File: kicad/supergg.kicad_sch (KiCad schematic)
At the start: 0 parts

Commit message: add pin connector holes
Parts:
- added U1: Cart_Connector, supergg:Cart_Connector, symbol supergg:Cart_Connector
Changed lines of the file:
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@@
 	(generator_version "9.0")
 	(paper "A4")
+	(symbol
+		(lib_id "supergg:Cart_Connector")
+		(at 72.39 88.9 0)
+		(unit 1)
+		(exclude_from_sim no)
+		(in_bom yes)
+		(on_board yes)
+		(dnp no)
+		(fields_autoplaced yes)
+		(property "Reference" "U1"
+			(at 72.39 35.56 0)
+			(effects
+				(font
+					(size 1.27 1.27)
+				)
+			)
+		)
+		(property "Value" "Cart_Connector"
+			(at 72.39 38.1 0)
+			(effects
+				(font
+					(size 1.27 1.27)
+				)
+			)
+		)
+		(property "Footprint" "supergg:Cart_Connector"
+			(at 72.39 88.9 0)
+			(effects
+				(font
+					(size 1.27 1.27)
+				)
+				(hide yes)
+			)
+		)
+		(property "Datasheet" ""
+			(at 72.39 88.9 0)
+			(effects
+				(font
+					(size 1.27 1.27)
+				)
+				(hide yes)
+			)
+		)
+		(property "Description" ""
+			(at 72.39 88.9 0)
+			(effects
+				(font
+					(size 1.27 1.27)
+				)
+				(hide yes)
+			)
+		)
+		(pin "46"
+		)
+		(pin "52"
+		)
+		(pin "8"
+		)
+		(pin "61"
+		)
+		(pin "69"
+		)
+		(pin "28"
+		)
+		(pin "24"
+		)
+		(pin "2"
+		)
+		(pin "3"
+		)
+		(pin "72"
+		)
+		(pin "33"
+		)
+		(pin "30"
+		)
+		(pin "22"
+		)
+		(pin "31"
+		)
+		(pin "34"
+		)
+		(pin "32"
+		)
+		(pin "35"
+		)
+		(pin "36"
+		)
+		(pin "59"
+		)
+		(pin "13"
+		)
+		(pin "1"
+		)
+		(pin "45"
+		)
+		(pin "70"
+		)
+		(pin "67"
+		)
+		(pin "44"
+		)
+		(pin "62"
+		)
+		(pin "20"
+		)
+		(pin "4"
+		)
+		(pin "63"
+		)
+		(pin "42"
+		)
+		(pin "7"
+		)
+		(pin "43"
+		)
+		(pin "53"
+		)
+		(pin "55"
+		)
+		(pin "18"
+		)
+		(pin "49"
+		)
+		(pin "48"
+		)
+		(pin "25"
+		)
+		(pin "12"
+		)
+		(pin "41"
+		)
+		(pin "14"
+		)
+		(pin "50"
+		)
+		(pin "16"
+		)
+		(pin "51"
+		)
+		(pin "47"
+		)
+		(pin "26"
+		)
+		(pin "15"
+		)
+		(pin "60"
+		)
+		(pin "23"
+		)
+		(pin "38"
+		)
+		(pin "54"
+		)
+		(pin "39"
+		)
+		(pin "65"
+		)
+		(pin "40"
+		)
+		(pin "68"
+		)
+		(pin "57"
+		)
+		(pin "58"
+		)
+		(pin "66"
+		)
+		(pin "19"
+		)
+		(pin "9"
+		)
+		(pin "11"
+		)
+		(pin "71"
+		)
+		(pin "10"
+		)
+		(pin "5"
+		)
+		(pin "17"
+		)
+		(pin "21"
+		)
+		(pin "29"
+		)
+		(pin "6"
+		)
+		(pin "27"
+		)
+		(pin "37"
+		)
+		(pin "64"
+		)
+		(pin "56"
+		)
+		(instances
+			(project ""
+				(path "/b7e908d3-ce0c-4aa7-87ef-800cbc8c6f17"
+					(reference "U1")
+					(unit 1)
+				)
+			)
+		)
+	)
 	(sheet_instances
 		(path "/"

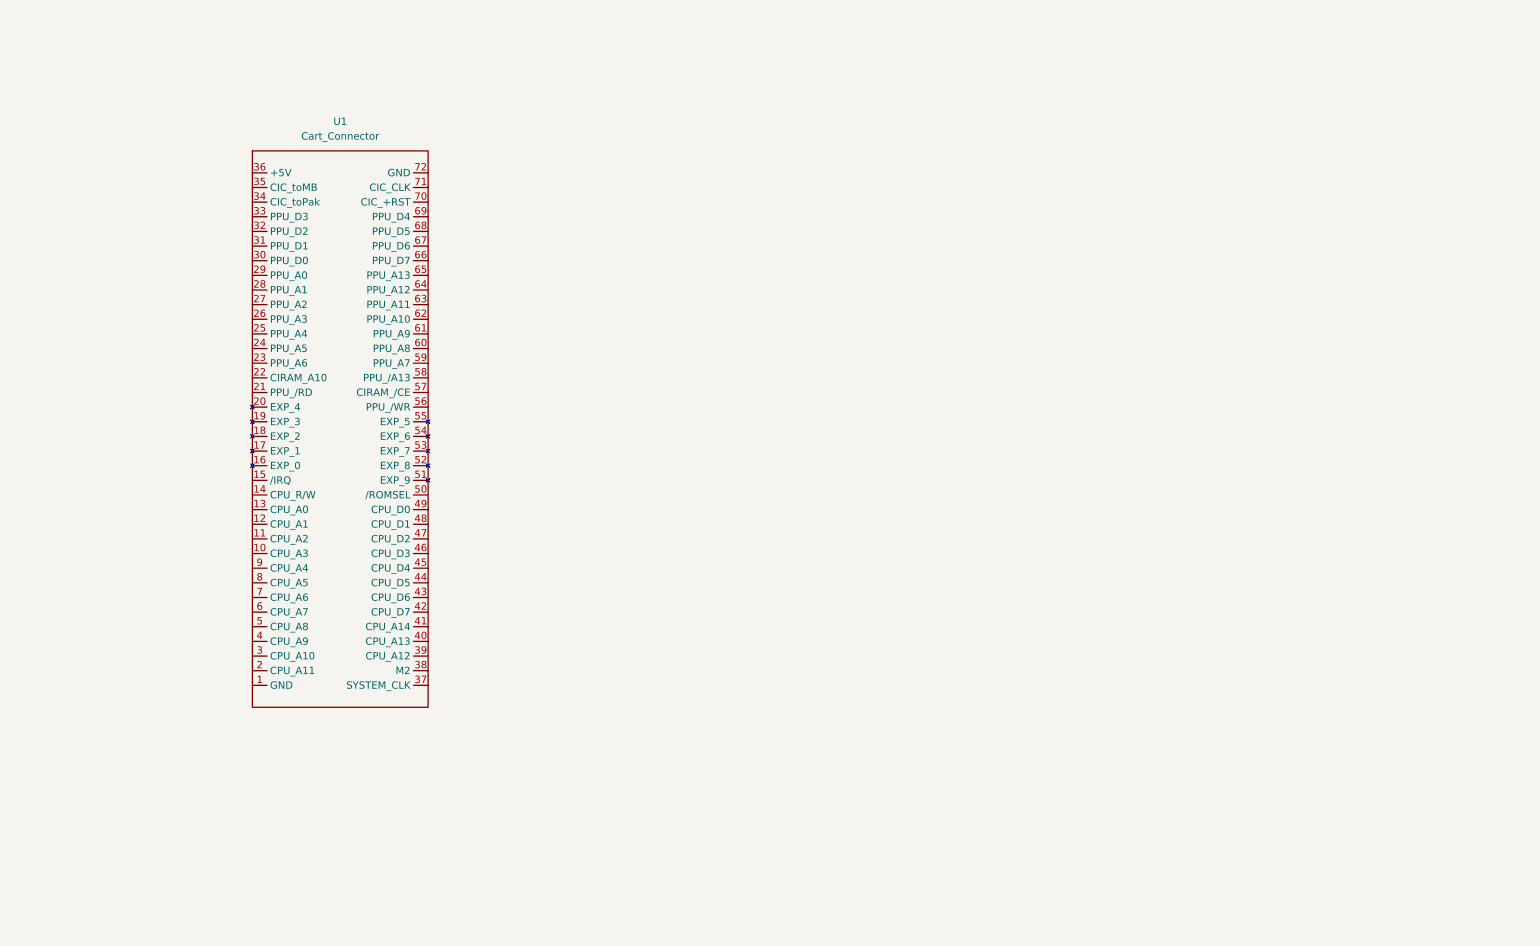
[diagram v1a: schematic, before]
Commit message: add edge connector symbol
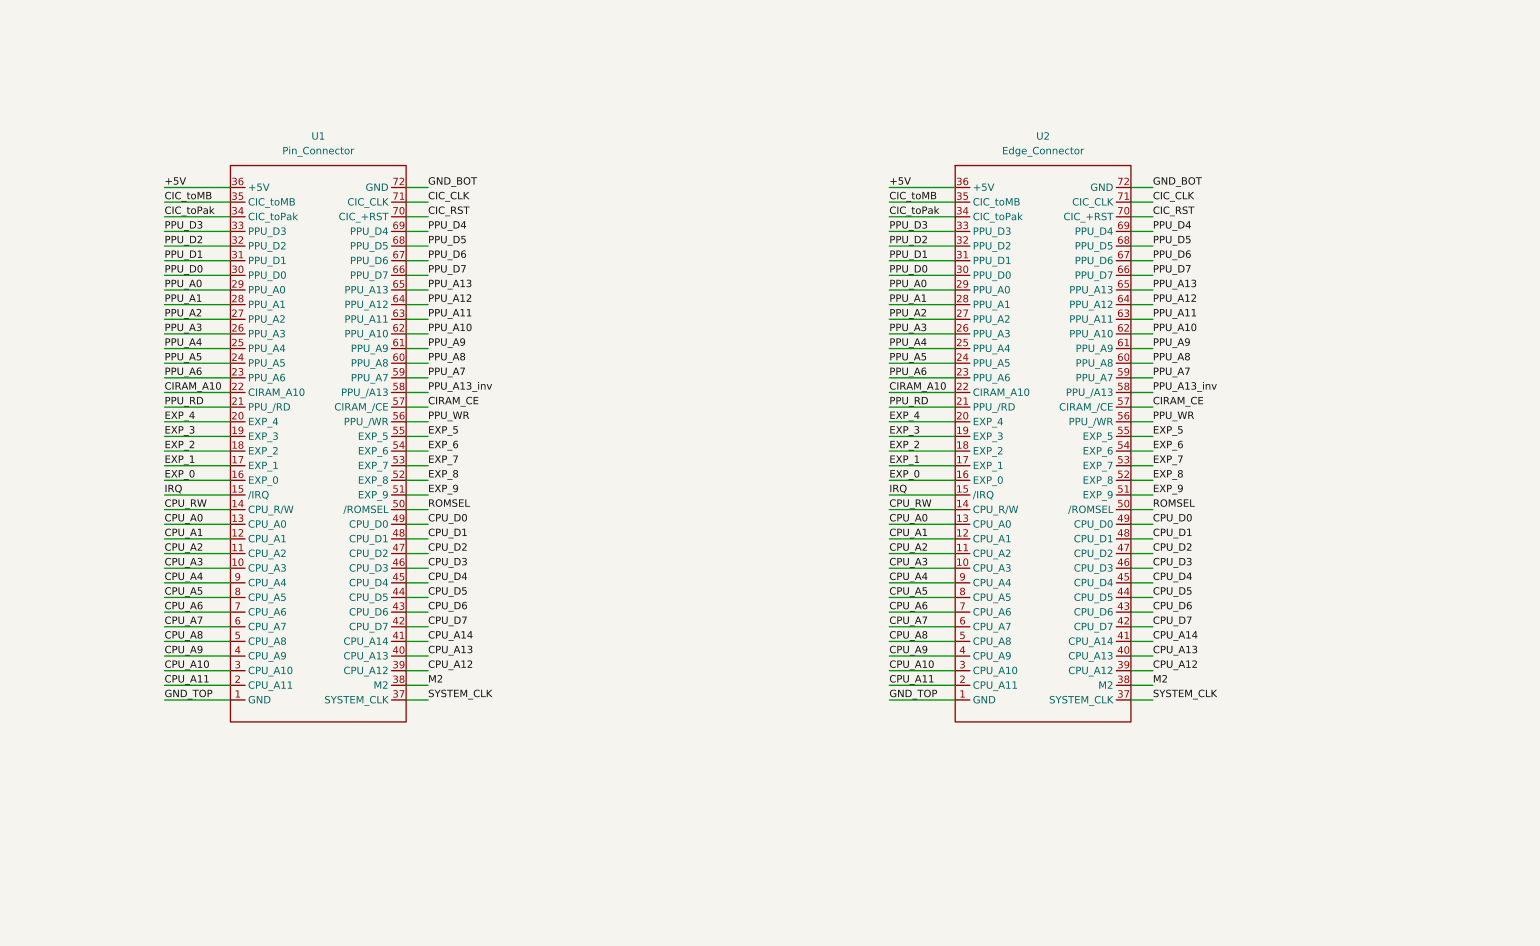
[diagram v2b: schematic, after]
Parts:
- removed U1: Cart_Connector, supergg:Cart_Connector, symbol supergg:Cart_Connector
- added U1: Pin_Connector, symbol supergg:Pin_Connector
- added U2: Edge_Connector, symbol supergg:Edge_Connector
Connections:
- new net +5V: U1.36 (+5V), U2.36 (+5V)
- new net CIC_CLK: U1.71 (CIC_CLK), U2.71 (CIC_CLK)
- new net CIC_RST: U1.70 (CIC_+RST), U2.70 (CIC_+RST)
- new net CIC_toMB: U1.35 (CIC_toMB), U2.35 (CIC_toMB)
- new net CIC_toPak: U1.34 (CIC_toPak), U2.34 (CIC_toPak)
- new net CIRAM_A10: U1.22 (CIRAM_A10), U2.22 (CIRAM_A10)
- new net CIRAM_CE: U1.57 (CIRAM_/CE), U2.57 (CIRAM_/CE)
- new net CPU_A0: U1.13 (CPU_A0), U2.13 (CPU_A0)
- new net CPU_A1: U1.12 (CPU_A1), U2.12 (CPU_A1)
- new net CPU_A10: U1.3 (CPU_A10), U2.3 (CPU_A10)
- new net CPU_A11: U1.2 (CPU_A11), U2.2 (CPU_A11)
- new net CPU_A12: U1.39 (CPU_A12), U2.39 (CPU_A12)
- new net CPU_A13: U1.40 (CPU_A13), U2.40 (CPU_A13)
- new net CPU_A14: U1.41 (CPU_A14), U2.41 (CPU_A14)
- new net CPU_A2: U1.11 (CPU_A2), U2.11 (CPU_A2)
- new net CPU_A3: U1.10 (CPU_A3), U2.10 (CPU_A3)
- new net CPU_A4: U1.9 (CPU_A4), U2.9 (CPU_A4)
- new net CPU_A5: U1.8 (CPU_A5), U2.8 (CPU_A5)
- new net CPU_A6: U1.7 (CPU_A6), U2.7 (CPU_A6)
- new net CPU_A7: U1.6 (CPU_A7), U2.6 (CPU_A7)
- new net CPU_A8: U1.5 (CPU_A8), U2.5 (CPU_A8)
- new net CPU_A9: U1.4 (CPU_A9), U2.4 (CPU_A9)
- new net CPU_D0: U1.49 (CPU_D0), U2.49 (CPU_D0)
- new net CPU_D1: U1.48 (CPU_D1), U2.48 (CPU_D1)
- new net CPU_D2: U1.47 (CPU_D2), U2.47 (CPU_D2)
- new net CPU_D3: U1.46 (CPU_D3), U2.46 (CPU_D3)
- new net CPU_D4: U1.45 (CPU_D4), U2.45 (CPU_D4)
- new net CPU_D5: U1.44 (CPU_D5), U2.44 (CPU_D5)
- new net CPU_D6: U1.43 (CPU_D6), U2.43 (CPU_D6)
- new net CPU_D7: U1.42 (CPU_D7), U2.42 (CPU_D7)
- new net CPU_RW: U1.14 (CPU_R/W), U2.14 (CPU_R/W)
- new net EXP_0: U1.16 (EXP_0), U2.16 (EXP_0)
- new net EXP_1: U1.17 (EXP_1), U2.17 (EXP_1)
- new net EXP_2: U1.18 (EXP_2), U2.18 (EXP_2)
- new net EXP_3: U1.19 (EXP_3), U2.19 (EXP_3)
- new net EXP_4: U1.20 (EXP_4), U2.20 (EXP_4)
- new net EXP_5: U1.55 (EXP_5), U2.55 (EXP_5)
- new net EXP_6: U1.54 (EXP_6), U2.54 (EXP_6)
- new net EXP_7: U1.53 (EXP_7), U2.53 (EXP_7)
- new net EXP_8: U1.52 (EXP_8), U2.52 (EXP_8)
- new net EXP_9: U1.51 (EXP_9), U2.51 (EXP_9)
- new net GND_BOT: U1.72 (GND), U2.72 (GND)
- new net GND_TOP: U1.1 (GND), U2.1 (GND)
- new net IRQ: U1.15 (/IRQ), U2.15 (/IRQ)
- new net M2: U1.38 (M2), U2.38 (M2)
- new net PPU_A0: U1.29 (PPU_A0), U2.29 (PPU_A0)
- new net PPU_A1: U1.28 (PPU_A1), U2.28 (PPU_A1)
- new net PPU_A10: U1.62 (PPU_A10), U2.62 (PPU_A10)
- new net PPU_A11: U1.63 (PPU_A11), U2.63 (PPU_A11)
- new net PPU_A12: U1.64 (PPU_A12), U2.64 (PPU_A12)
- new net PPU_A13: U1.65 (PPU_A13), U2.65 (PPU_A13)
- new net PPU_A13_inv: U1.58 (PPU_/A13), U2.58 (PPU_/A13)
- new net PPU_A2: U1.27 (PPU_A2), U2.27 (PPU_A2)
- new net PPU_A3: U1.26 (PPU_A3), U2.26 (PPU_A3)
- new net PPU_A4: U1.25 (PPU_A4), U2.25 (PPU_A4)
- new net PPU_A5: U1.24 (PPU_A5), U2.24 (PPU_A5)
- new net PPU_A6: U1.23 (PPU_A6), U2.23 (PPU_A6)
- new net PPU_A7: U1.59 (PPU_A7), U2.59 (PPU_A7)
- new net PPU_A8: U1.60 (PPU_A8), U2.60 (PPU_A8)
- new net PPU_A9: U1.61 (PPU_A9), U2.61 (PPU_A9)
- new net PPU_D0: U1.30 (PPU_D0), U2.30 (PPU_D0)
- new net PPU_D1: U1.31 (PPU_D1), U2.31 (PPU_D1)
- new net PPU_D2: U1.32 (PPU_D2), U2.32 (PPU_D2)
- new net PPU_D3: U1.33 (PPU_D3), U2.33 (PPU_D3)
- new net PPU_D4: U1.69 (PPU_D4), U2.69 (PPU_D4)
- new net PPU_D5: U1.68 (PPU_D5), U2.68 (PPU_D5)
- new net PPU_D6: U1.67 (PPU_D6), U2.67 (PPU_D6)
- new net PPU_D7: U1.66 (PPU_D7), U2.66 (PPU_D7)
- new net PPU_RD: U1.21 (PPU_/RD), U2.21 (PPU_/RD)
- new net PPU_WR: U1.56 (PPU_/WR), U2.56 (PPU_/WR)
- new net ROMSEL: U1.50 (/ROMSEL), U2.50 (/ROMSEL)
- new net SYSTEM_CLK: U1.37 (SYSTEM_CLK), U2.37 (SYSTEM_CLK)

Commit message: add edge connector footprint
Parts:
- U1: footprint (none) -> supergg:Pin_Connector
- U2: footprint (none) -> supergg:Edge_Connector
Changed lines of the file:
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@@
 			)
 		)
-		(property "Footprint" ""
+		(property "Footprint" "supergg:Pin_Connector"
 			(at 68.58 91.44 0)
 			(effects
@@
 			)
 		)
-		(property "Footprint" ""
+		(property "Footprint" "supergg:Edge_Connector"
 			(at 194.31 91.44 0)
 			(effects

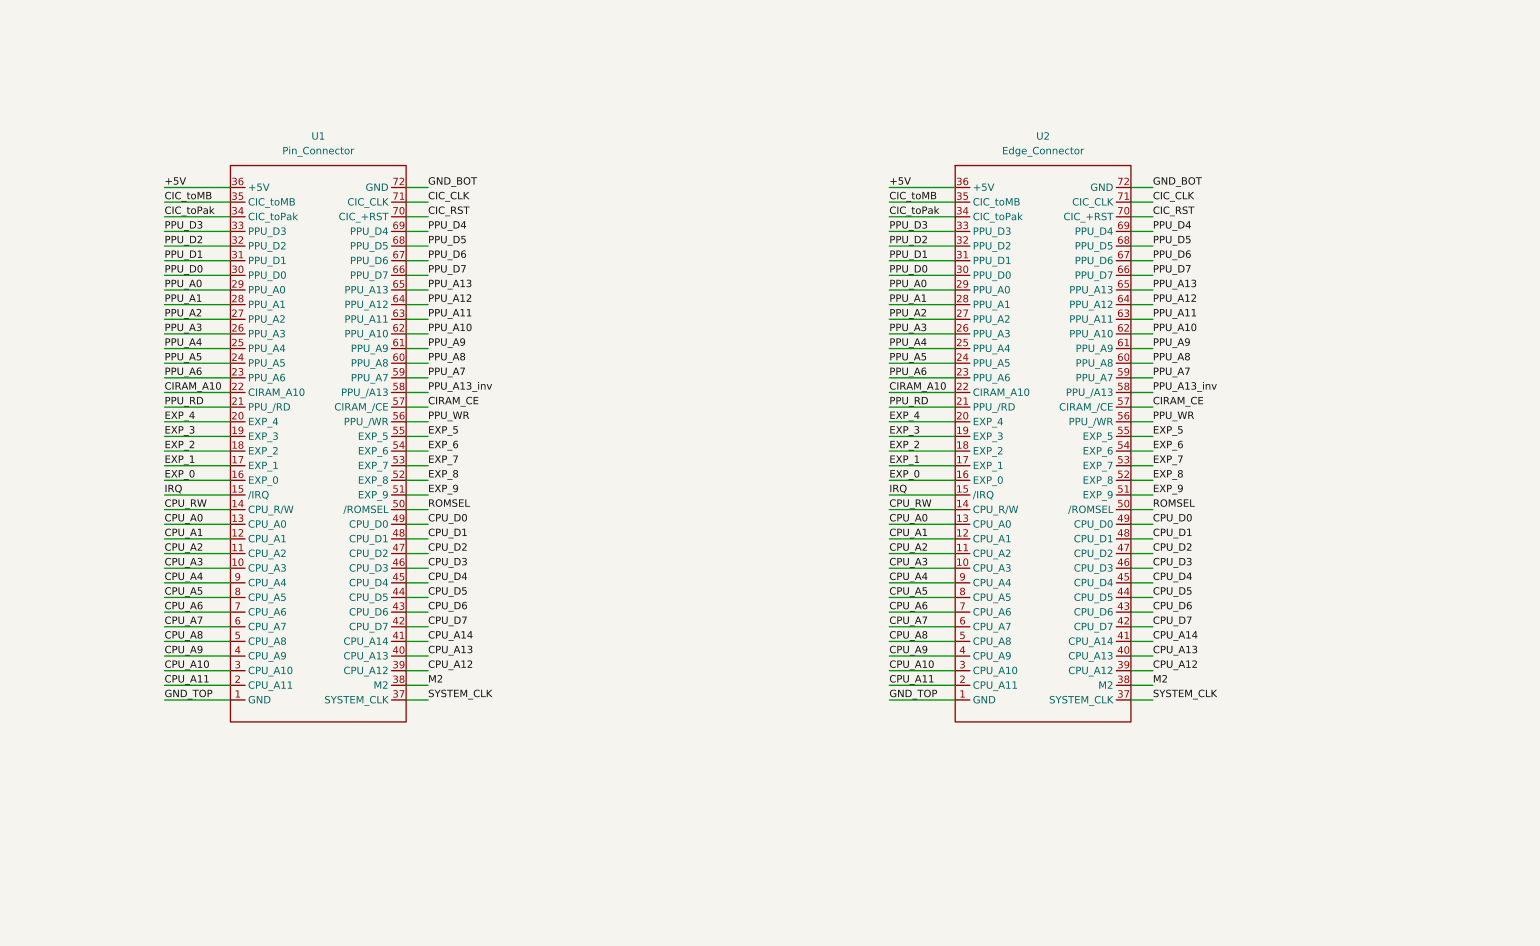
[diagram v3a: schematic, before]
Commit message: add symbols and footprints for most parts
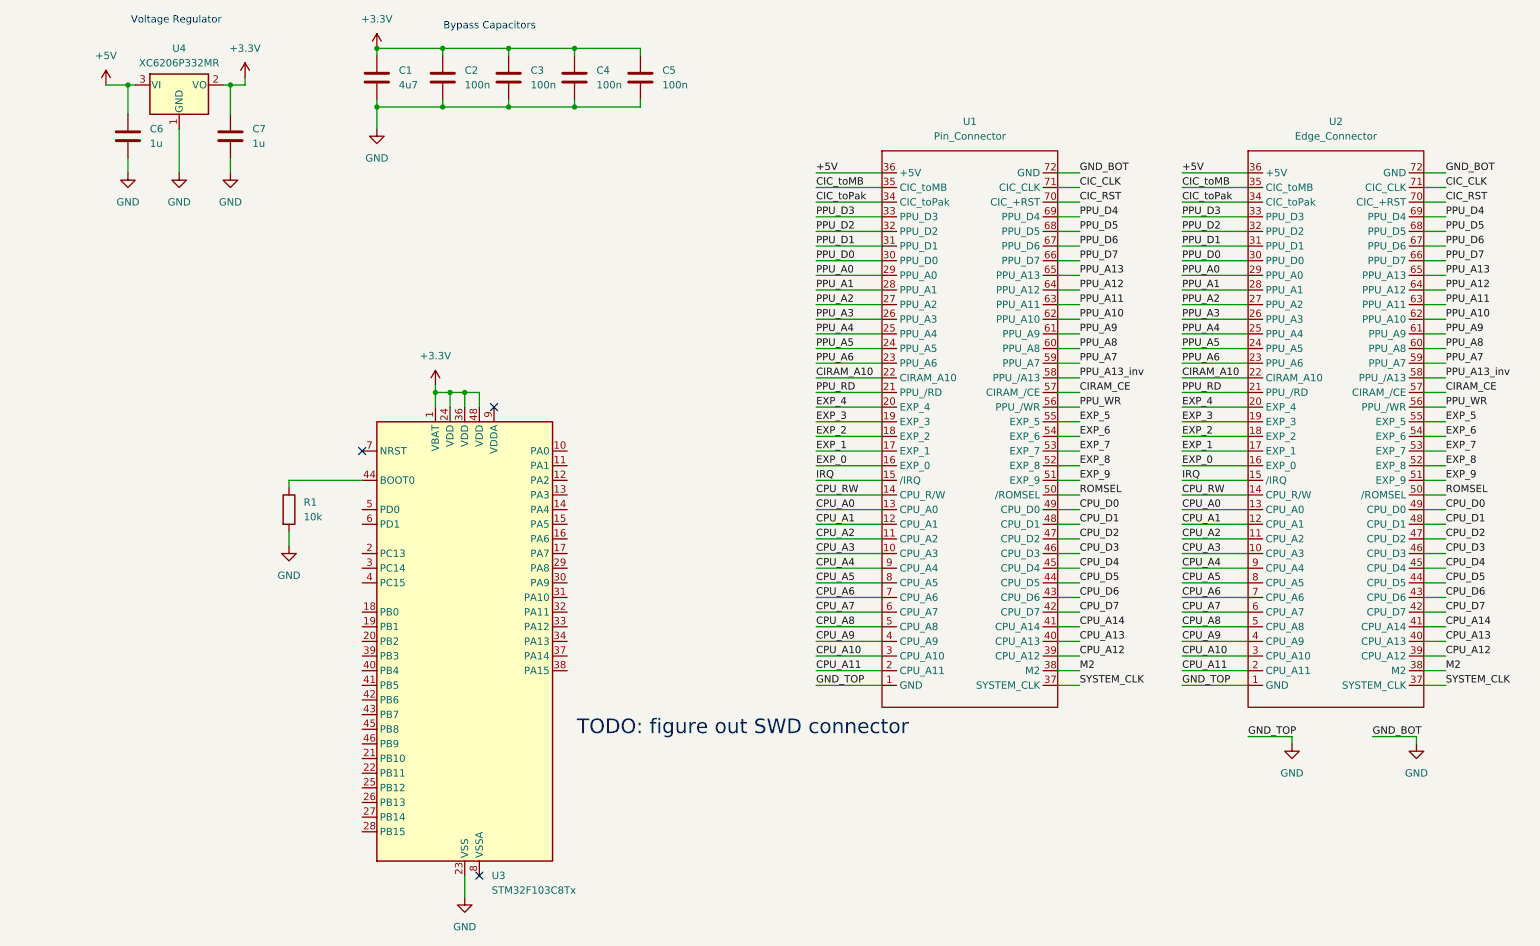
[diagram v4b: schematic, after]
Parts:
- added C1: 4u7, Capacitor_SMD:C_0603_1608Metric, symbol Device:C
- added C2, C3, C4, C5: 100n, Capacitor_SMD:C_0402_1005Metric, symbol Device:C
- added C6, C7: 1u, Capacitor_SMD:C_0603_1608Metric, symbol Device:C
- added R1: 10k, Resistor_SMD:R_0603_1608Metric, symbol Device:R
- added U3: STM32F103C8Tx, Package_QFP:LQFP-48_7x7mm_P0.5mm, symbol MCU_ST_STM32F1:STM32F103C8Tx
- added U4: XC6206P332MR, Package_TO_SOT_SMD:SOT-23-3, symbol Regulator_Linear:XC6206PxxxMR
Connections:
- net GND_TOP is gone; now on net GND: U1.1 (GND), U2.1 (GND)
- net +5V: now also C6.1, U4.3 (VI)
- net GND_BOT renamed GND
- net GND: now also C1.2, C2.2, C3.2, C4.2, C5.2, C6.2, C7.2, R1.2, U3.23 (VSS), U3.35 (VSS), U3.47 (VSS), U4.1 (GND)
- new net: R1.1, U3.44 (BOOT0)
- new net +3.3V: C1.1, C2.1, C3.1, C4.1, C5.1, C7.1, U3.1 (VBAT), U3.24 (VDD), U3.36 (VDD), U3.48 (VDD), U4.2 (VO)
- no-connect marks 0 -> 3
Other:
- note added: "Bypass Capacitors"
- note added: "TODO: figure out SWD connector"
- note added: "Voltage Regulator"
- moved on the sheet: U1, U2

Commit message: rework wiring
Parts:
- added J1: Conn_01x04_Pin, Connector_PinHeader_2.54mm:PinHeader_1x04_P2.54mm_Horizontal, symbol Connector:Conn_01x04_Pin
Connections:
- net GND: now also J1.1 (Pin_1)
- net SWDIO: now reaches U3.34 (PA13)
- net SWDIO: now also J1.4 (Pin_4)
- net SWDCLK: now reaches U3.37 (PA14)
- net SWDCLK: now also J1.3 (Pin_3)
- net SWO: now reaches U3.39 (PB3)
- net SWO: now also J1.2 (Pin_2)
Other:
- note added: "SWD Connector"
- moved on the sheet: R1, U3
